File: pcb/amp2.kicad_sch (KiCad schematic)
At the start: 16 parts, among them Q3 BFP640

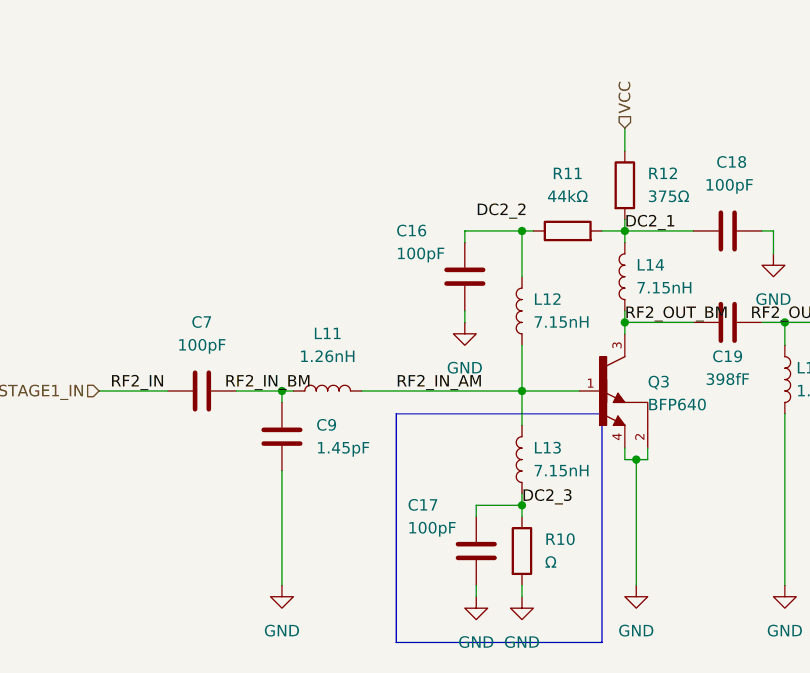
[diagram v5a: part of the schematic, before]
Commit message: PCB modified according to suggestions
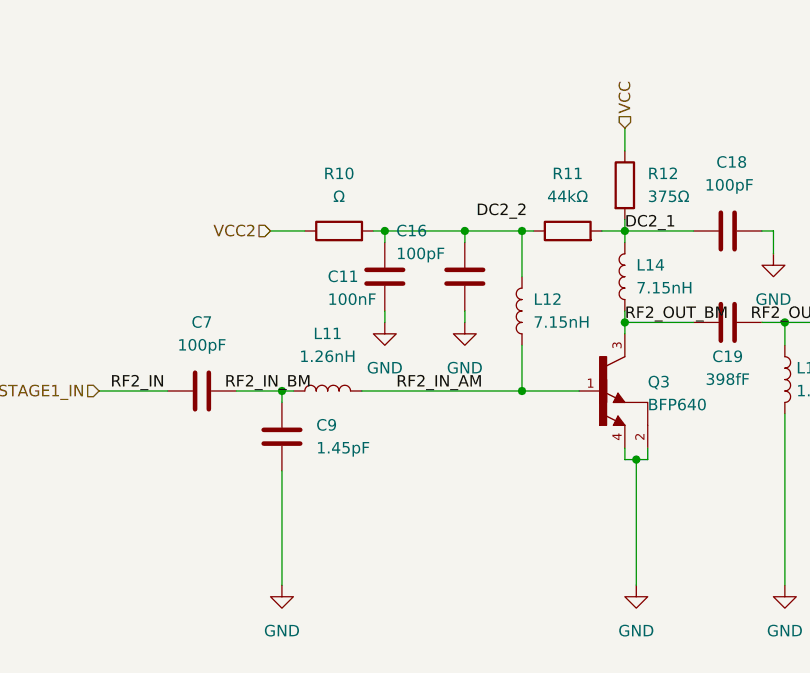
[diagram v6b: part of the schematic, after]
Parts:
- removed C17: 100pF, Capacitor_SMD:C_0603_1608Metric, symbol Device:C
- removed L13: 7.15nH, Nicobigio01:Coilcraft_1606-xxLx, symbol Device:L
- added C11: 100nF, Capacitor_SMD:C_1206_3216Metric, symbol Device:C
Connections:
- net GND: now also C11.2; no longer R10.2
- net at C16.1, L12.2, R11.1: now also R10.2, C11.1
- net DC2_3 renamed VCC2
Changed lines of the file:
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@@
   (junction (at 158.75 99.06) (diameter 0) (color 0 0 0 0)
   )
+  (junction (at 130.81 73.66) (diameter 0) (color 0 0 0 0)
+  )
   (junction (at 157.48 73.66) (diameter 0) (color 0 0 0 0)
   )
+  (junction (at 139.7 73.66) (diameter 0) (color 0 0 0 0)
+  )
   (junction (at 146.05 91.44) (diameter 0) (color 0 0 0 0)
   )
@@
   (junction (at 146.05 73.66) (diameter 0) (color 0 0 0 0)
   )
-  (junction (at 146.05 104.14) (diameter 0) (color 0 0 0 0)
-  )
   (junction (at 157.48 83.82) (diameter 0) (color 0 0 0 0)
   )
@@
     (stroke (width 0) (type default) (color 0 0 0 0))
   )
+  (wire (pts (xy 130.81 73.66) (xy 139.7 73.66))
+    (stroke (width 0) (type default) (color 0 0 0 0))
+  )
   (wire (pts (xy 99.06 91.44) (xy 106.68 91.44))
     (stroke (width 0) (type default) (color 0 0 0 0))
   )
-  (wire (pts (xy 140.97 105.41) (xy 140.97 104.14))
-    (stroke (width 0) (type default) (color 0 0 0 0))
-  )
   (wire (pts (xy 157.48 62.23) (xy 157.48 64.77))
     (stroke (width 0) (type default) (color 0 0 0 0))
@@
     (stroke (width 0) (type default) (color 0 0 0 0))
   )
-  (wire (pts (xy 140.97 113.03) (xy 140.97 114.3))
-    (stroke (width 0) (type default) (color 0 0 0 0))
-  )
   (wire (pts (xy 175.26 93.98) (xy 175.26 113.03))
     (stroke (width 0) (type default) (color 0 0 0 0))
@@
     (stroke (width 0) (type default) (color 0 0 0 0))
   )
-  (wire (pts (xy 146.05 104.14) (xy 146.05 105.41))
-    (stroke (width 0) (type default) (color 0 0 0 0))
-  )
   (wire (pts (xy 146.05 73.66) (xy 147.32 73.66))
     (stroke (width 0) (type default) (color 0 0 0 0))
   )
+  (wire (pts (xy 130.81 82.55) (xy 130.81 83.82))
+    (stroke (width 0) (type default) (color 0 0 0 0))
+  )
   (wire (pts (xy 172.72 83.82) (xy 175.26 83.82))
     (stroke (width 0) (type default) (color 0 0 0 0))
   )
-  (wire (pts (xy 146.05 113.03) (xy 146.05 114.3))
+  (wire (pts (xy 130.81 74.93) (xy 130.81 73.66))
     (stroke (width 0) (type default) (color 0 0 0 0))
   )
@@
     (stroke (width 0) (type default) (color 0 0 0 0))
   )
+  (wire (pts (xy 118.11 73.66) (xy 121.92 73.66))
+    (stroke (width 0) (type default) (color 0 0 0 0))
+  )
   (wire (pts (xy 175.26 83.82) (xy 175.26 86.36))
     (stroke (width 0) (type default) (color 0 0 0 0))
   )
-  (polyline (pts (xy 132.08 93.98) (xy 132.08 119.38))
-    (stroke (width 0) (type default) (color 0 0 0 0))
-  )
-  (wire (pts (xy 140.97 104.14) (xy 146.05 104.14))
-    (stroke (width 0) (type default) (color 0 0 0 0))
-  )
-  (wire (pts (xy 146.05 91.44) (xy 146.05 95.25))
-    (stroke (width 0) (type default) (color 0 0 0 0))
-  )
-  (wire (pts (xy 146.05 102.87) (xy 146.05 104.14))
-    (stroke (width 0) (type default) (color 0 0 0 0))
-  )
   (wire (pts (xy 139.7 74.93) (xy 139.7 73.66))
     (stroke (width 0) (type default) (color 0 0 0 0))
@@
     (stroke (width 0) (type default) (color 0 0 0 0))
   )
+  (wire (pts (xy 129.54 73.66) (xy 130.81 73.66))
+    (stroke (width 0) (type default) (color 0 0 0 0))
+  )
   (wire (pts (xy 128.27 91.44) (xy 146.05 91.44))
     (stroke (width 0) (type default) (color 0 0 0 0))
@@
     (stroke (width 0) (type default) (color 0 0 0 0))
   )
-  (polyline (pts (xy 132.08 93.98) (xy 154.94 93.98))
-    (stroke (width 0) (type default) (color 0 0 0 0))
-  )
-  (polyline (pts (xy 154.94 93.98) (xy 154.94 119.38))
-    (stroke (width 0) (type default) (color 0 0 0 0))
-  )
   (wire (pts (xy 173.99 73.66) (xy 173.99 76.2))
     (stroke (width 0) (type default) (color 0 0 0 0))
@@
   )
   (wire (pts (xy 157.48 72.39) (xy 157.48 73.66))
-    (stroke (width 0) (type default) (color 0 0 0 0))
-  )
-  (polyline (pts (xy 154.94 119.38) (xy 132.08 119.38))
     (stroke (width 0) (type default) (color 0 0 0 0))
   )
@@
     (effects (font (size 1.27 1.27)) (justify left bottom))
   )
-  (label "DC2_3" (at 146.05 104.14 0)
-    (effects (font (size 1.27 1.27)) (justify left bottom))
-  )
   (label "RF2_OUT_AM" (at 171.45 83.82 0)
     (effects (font (size 1.27 1.27)) (justify left bottom))
@@
     (effects (font (size 1.27 1.27)) (justify right))
   )
+  (hierarchical_label "VCC2" (shape input) (at 118.11 73.66 180)
+    (effects (font (size 1.27 1.27)) (justify right))
+  )
   (hierarchical_label "VCC" (shape input) (at 157.48 62.23 90)
     (effects (font (size 1.27 1.27)) (justify left))
   )
-  (symbol (lib_id "Device:R") (at 146.05 109.22 0) (unit 1)
-    (in_bom yes) (on_board yes) (fields_autoplaced)
-    (property "Reference" "R10" (id 0) (at 148.59 107.9499 0)
-      (effects (font (size 1.27 1.27)) (justify left))
-    )
-    (property "Value" "Ω" (id 1) (at 148.59 110.4899 0)
-      (effects (font (size 1.27 1.27)) (justify left))
-    )
-    (property "Footprint" "Resistor_SMD:R_0603_1608Metric" (id 2) (at 144.272 109.22 90)
-      (effects (font (size 1.27 1.27)) hide)
-    )
-    (property "Datasheet" "~" (id 3) (at 146.05 109.22 0)
-      (effects (font (size 1.27 1.27)) hide)
-    )
-    (pin "1")
-    (pin "2")
-  )
   (symbol (lib_id "Device:L") (at 175.26 90.17 0) (unit 1)
     (in_bom yes) (on_board yes) (fields_autoplaced)
@@
     (pin "2")
   )
-  (symbol (lib_id "power:GND") (at 146.05 114.3 0) (unit 1)
-    (in_bom yes) (on_board yes) (fields_autoplaced)
-    (property "Reference" "#PWR0127" (id 0) (at 146.05 120.65 0)
-      (effects (font (size 1.27 1.27)) hide)
-    )
-    (property "Value" "GND" (id 1) (at 146.05 119.38 0))
-    (property "Footprint" "" (id 2) (at 146.05 114.3 0)
-      (effects (font (size 1.27 1.27)) hide)
-    )
-    (property "Datasheet" "" (id 3) (at 146.05 114.3 0)
-      (effects (font (size 1.27 1.27)) hide)
-    )
-    (pin "1")
+  (symbol (lib_id "Device:R") (at 125.73 73.66 90) (unit 1)
+    (in_bom yes) (on_board yes) (fields_autoplaced)
+    (property "Reference" "R10" (id 0) (at 125.73 67.31 90))
+    (property "Value" "Ω" (id 1) (at 125.73 69.85 90))
+    (property "Footprint" "Resistor_SMD:R_0603_1608Metric" (id 2) (at 125.73 75.438 90)
+      (effects (font (size 1.27 1.27)) hide)
+    )
+    (property "Datasheet" "~" (id 3) (at 125.73 73.66 0)
+      (effects (font (size 1.27 1.27)) hide)
+    )
+    (pin "1")
+    (pin "2")
   )
   (symbol (lib_id "Nicobigio01_Transistor_HBT:BFP640") (at 154.94 91.44 0) (unit 1)
@@
     (pin "2")
   )
-  (symbol (lib_id "Device:C") (at 140.97 109.22 0) (mirror y) (unit 1)
-    (in_bom yes) (on_board yes)
-    (property "Reference" "C17" (id 0) (at 133.35 104.14 0)
-      (effects (font (size 1.27 1.27)) (justify right))
-    )
-    (property "Value" "100pF" (id 1) (at 133.35 106.68 0)
-      (effects (font (size 1.27 1.27)) (justify right))
-    )
-    (property "Footprint" "Capacitor_SMD:C_0603_1608Metric" (id 2) (at 140.0048 113.03 0)
-      (effects (font (size 1.27 1.27)) hide)
-    )
-    (property "Datasheet" "~" (id 3) (at 140.97 109.22 0)
-      (effects (font (size 1.27 1.27)) hide)
-    )
-    (pin "1")
-    (pin "2")
-  )
   (symbol (lib_id "power:GND") (at 158.75 113.03 0) (unit 1)
     (in_bom yes) (on_board yes) (fields_autoplaced)
@@
     (pin "1")
     (pin "2")
+  )
+  (symbol (lib_id "power:GND") (at 130.81 83.82 0) (unit 1)
+    (in_bom yes) (on_board yes) (fields_autoplaced)
+    (property "Reference" "#PWR0114" (id 0) (at 130.81 90.17 0)
+      (effects (font (size 1.27 1.27)) hide)
+    )
+    (property "Value" "GND" (id 1) (at 130.81 88.9 0))
+    (property "Footprint" "" (id 2) (at 130.81 83.82 0)
+      (effects (font (size 1.27 1.27)) hide)
+    )
+    (property "Datasheet" "" (id 3) (at 130.81 83.82 0)
+      (effects (font (size 1.27 1.27)) hide)
+    )
+    (pin "1")
   )
   (symbol (lib_id "Device:C") (at 168.91 83.82 90) (unit 1)
@@
     (pin "2")
   )
+  (symbol (lib_id "Device:C") (at 130.81 78.74 0) (mirror y) (unit 1)
+    (in_bom yes) (on_board yes)
+    (property "Reference" "C11" (id 0) (at 124.46 78.74 0)
+      (effects (font (size 1.27 1.27)) (justify right))
+    )
+    (property "Value" "100nF" (id 1) (at 124.46 81.28 0)
+      (effects (font (size 1.27 1.27)) (justify right))
+    )
+    (property "Footprint" "Capacitor_SMD:C_1206_3216Metric" (id 2) (at 129.8448 82.55 0)
+      (effects (font (size 1.27 1.27)) hide)
+    )
+    (property "Datasheet" "~" (id 3) (at 130.81 78.74 0)
+      (effects (font (size 1.27 1.27)) hide)
+    )
+    (pin "1")
+    (pin "2")
+  )
   (symbol (lib_id "Device:L") (at 146.05 82.55 180) (unit 1)
     (in_bom yes) (on_board yes) (fields_autoplaced)
@@
     (pin "2")
   )
-  (symbol (lib_id "Device:L") (at 146.05 99.06 180) (unit 1)
-    (in_bom yes) (on_board yes) (fields_autoplaced)
-    (property "Reference" "L13" (id 0) (at 147.32 97.7899 0)
-      (effects (font (size 1.27 1.27)) (justify right))
-    )
-    (property "Value" "7.15nH" (id 1) (at 147.32 100.3299 0)
-      (effects (font (size 1.27 1.27)) (justify right))
-    )
-    (property "Footprint" "Nicobigio01:Coilcraft_1606-xxLx" (id 2) (at 146.05 99.06 0)
-      (effects (font (size 1.27 1.27)) hide)
-    )
-    (property "Datasheet" "~" (id 3) (at 146.05 99.06 0)
-      (effects (font (size 1.27 1.27)) hide)
-    )
-    (pin "1")
-    (pin "2")
-  )
   (symbol (lib_id "Device:C") (at 168.91 73.66 90) (mirror x) (unit 1)
     (in_bom yes) (on_board yes)
@@
     (pin "2")
   )
-  (symbol (lib_id "power:GND") (at 140.97 114.3 0) (unit 1)
-    (in_bom yes) (on_board yes) (fields_autoplaced)
-    (property "Reference" "#PWR0126" (id 0) (at 140.97 120.65 0)
-      (effects (font (size 1.27 1.27)) hide)
-    )
-    (property "Value" "GND" (id 1) (at 140.97 119.38 0))
-    (property "Footprint" "" (id 2) (at 140.97 114.3 0)
-      (effects (font (size 1.27 1.27)) hide)
-    )
-    (property "Datasheet" "" (id 3) (at 140.97 114.3 0)
-      (effects (font (size 1.27 1.27)) hide)
-    )
-    (pin "1")
-  )
   (symbol (lib_id "Device:C") (at 139.7 78.74 0) (mirror y) (unit 1)
